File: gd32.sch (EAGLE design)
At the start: 23 parts, among them IC1 GD32F450IKH6, IC2 AMS1117-1.5, J1 LCD, U1 W9825G6KH-5

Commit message: Incremental changes
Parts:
- added BOOT_SEL: B3F-1005, SparkFun:TAC_SWITCHPTH
- added BOOT_WHICH: JS202011SCQN, samacsys:JS202011SCQN
- added C10, C9: 10uF/16v, rcl:C-EUC0603
- added C11: 0.1uF, rcl:C-EUC0201
- added D1: GRN-0402, Seeed-LED:SMD-LED-CLEAR-BLUE(0402)
- added JP2: (no value), pinhead:PINHD-1X2
- added R4: 470R, rcl:R-EU_R0402
- added R5: 10K, rcl:R-EU_R0402
- added U$1: GD32_DEBUG, sjg-stm32:GD32_DEBUG
- IC2: value AMS1117-1.5 -> AMS1117-3.3
- renumbered POWER1 to +5V_IN
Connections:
- new net BOOT0: BOOT_SEL.3, BOOT_SEL.4, IC1.BOOT0, R5.2
- new net N$2: D1.+, R4.2
- new net N$3: C10.1, IC2.TAB, IC2.VOUT, JP2.2, R4.1
- net +3V3: now also BOOT_SEL.1, BOOT_SEL.2, BOOT_WHICH.1, BOOT_WHICH.6, JP2.1, U$1.VDD_OUT@1; no longer IC2.TAB, IC2.VOUT
- net +5V: now also C9.1
- net GND: now also BOOT_WHICH.3, BOOT_WHICH.4, C10.2, C11.2, C9.2, R5.1, U$1.GND@3, U$1.GND@5, U$1.GND@9
- net PA13: now also U$1.SWDIO@2
- net PA14: now also U$1.SWD_CLK@4
- net PB10: now also U$1.USART_TX@6
- net PB11: now also U$1.USART_RX@8
- net PB2: now also BOOT_WHICH.2, BOOT_WHICH.5
- net PB4: now also C11.1, U$1.!RESET!@10
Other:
- moved on the sheet: C1, C2, C3, C4, C5, C6, C7, U1

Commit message: Ready for manufacture
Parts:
- removed C11: 0.1uF, rcl:C-EUC0201
- removed U$1: GD32_DEBUG, sjg-stm32:GD32_DEBUG
- added C12, C13: 15pF, rcl:C-EUC0201
- added C14, C15, C16, C17, C18, C19, C20, C21, C22, C23, C24, C25, C26, C27, C28, C34: 0.1uF, rcl:C-EUC0201
- added I2C1, SPI0, SPI1, SPI2: (no value), pinhead:PINHD-2X2
- added IO_EXT: (no value), pinhead:PINHD-2X20
- added PASS_RST: (no value), pinhead:PINHD-1X2
- added PROG: GD32_DEBUG, sjg-stm32:GD32_DEBUG
- added Q2: 8MHz, adafruit:XTAL-4-3225
- added R37, R8: 1K5, rcl:R-EU_R0603
- added R6, R7: 10K, rcl:R-EU_R0402
- added RESET: B3F-1005, SparkFun:TAC_SWITCHPTH
- R2, R3: device rcl:R-EU_R0805 -> rcl:R-EU_R0402; USE RMCF0805FT22R0 -> CR0402-JW-220GLF
- renumbered JP1 to BL_CTRL, JP2 to PASS_3V3
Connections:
- net PA11 renamed MCU_USB_N
- net PA12 renamed MCU_USB_P
- removed net PB4: C11.1, IC1.PB4, U$1.!RESET!@10
- removed net PD13: IC1.PD13
- removed net PE2: IC1.PE2
- removed net PE3: IC1.PE3
- removed net PG13: IC1.PG13
- removed net PG14: IC1.PG14, U1.!CAS
- removed net PG3: IC1.PG3
- removed net PG9: IC1.PG9
- removed net PH6: IC1.PH6
- removed net PH7: IC1.PH7
- removed net PI11: IC1.PI11
- new net !RST!: IC1.!RST!, PASS_RST.2, R7.1, RESET.3, RESET.4
- new net N$4: IC1.PDR_ON, R6.1
- new net N$5: PASS_RST.1, PROG.!RESET!@10
- net +3V3: now also C14.1, C15.1, C16.1, C17.1, C18.1, C19.1, C20.1, C21.1, C22.1, C23.1, C24.1, C25.1, C26.1, C27.1, C28.1, C34.1, I2C1.1, IC1.VBAT, IC1.VDD@C5, IC1.VDD@C7, IC1.VDD@C8, IC1.VDD@C9, IC1.VDD@F3, IC1.VDD@G13, IC1.VDD@G3, IC1.VDD@H13, IC1.VDD@J12, IC1.VDD@J13, IC1.VDD@K4, IC1.VDD@N10, IC1.VDD@N8, IC1.VDD@N9, IC1.VDDA, IC1.VREF+, IO_EXT.2, PROG.VDD_OUT@1, R37.2, R6.2, R7.2, R8.2; no longer U$1.VDD_OUT@1
- net +5V: now also IO_EXT.1
- net GND: now also C12.2, C13.2, C14.2, C15.2, C16.2, C17.2, C18.2, C19.2, C20.2, C21.2, C22.2, C23.2, C24.2, C25.2, C26.2, C27.2, C28.2, C34.2, D1.-, I2C1.3, IC1.VREF-, IC1.VSS@D5, IC1.VSS@D7, IC1.VSS@D8, IC1.VSS@D9, IC1.VSS@F10, IC1.VSS@F12, IC1.VSS@F2, IC1.VSS@F6, IC1.VSS@F7, IC1.VSS@F8, IC1.VSS@F9, IC1.VSS@G10, IC1.VSS@G12, IC1.VSS@G2, IC1.VSS@G6, IC1.VSS@G7, IC1.VSS@G8, IC1.VSS@G9, IC1.VSS@H10, IC1.VSS@H12, IC1.VSS@H6, IC1.VSS@H7, IC1.VSS@H8, IC1.VSS@H9, IC1.VSS@J10, IC1.VSS@J6, IC1.VSS@J7, IC1.VSS@J8, IC1.VSS@J9, IC1.VSS@K10, IC1.VSS@K6, IC1.VSS@K7, IC1.VSS@K8, IC1.VSS@K9, IC1.VSS@M8, IC1.VSS@M9, IC1.VSSA, IO_EXT.19, IO_EXT.20, IO_EXT.39, IO_EXT.40, PROG.GND@3, PROG.GND@5, PROG.GND@9, Q2.G1, Q2.G2, RESET.1, RESET.2, SPI0.3, SPI1.3, SPI2.3; no longer C11.2, U$1.GND@3, U$1.GND@5, U$1.GND@9
- net PA0: now also IO_EXT.37
- net PA1: now also IO_EXT.38
- net PA13: now also PROG.SWDIO@2; no longer U$1.SWDIO@2
- net PA14: now also PROG.SWD_CLK@4; no longer U$1.SWD_CLK@4
- net PA15: now also IO_EXT.31
- net PA2: now also IO_EXT.35
- net PA3: now also IO_EXT.36
- net PA5: now also SPI0.2
- net PA6: now also SPI0.4
- net PA7: now also SPI0.1
- net PA8: now also IO_EXT.33
- net PA9: now also IO_EXT.34
- net PB0: now also IO_EXT.32
- net PB1: now also IO_EXT.29
- net PB10: now also PROG.USART_TX@6; no longer U$1.USART_TX@6
- net PB11: now also PROG.USART_RX@8; no longer U$1.USART_RX@8
- net PB12: now also IO_EXT.26
- net PB13: now also SPI1.2
- net PB14: now also SPI1.4
- net PB15: now also SPI1.1
- net PB3: now also IO_EXT.30
- net PB7: now also IO_EXT.27
- net PB8: now also IO_EXT.28
- net PB9: now also IO_EXT.25
- net PC0: now also IO_EXT.23
- net PC1: now also IO_EXT.24
- net PC10: now also SPI2.2
- net PC11: now also SPI2.4
- net PC12: now also SPI2.1
- net PC13: now also IO_EXT.11
- net PC14: now also IO_EXT.12
- net PC15: now also IO_EXT.9
- net PC2: now also IO_EXT.21
- net PC3: now also IO_EXT.22
- net PC4: now also IO_EXT.17
- net PC5: now also IO_EXT.18
- net PC6: now also IO_EXT.15
- net PC7: now also IO_EXT.16
- net PC8: now also IO_EXT.13
- net PC9: now also IO_EXT.14
- net PD11: now also IO_EXT.3
- net PD12: now also IO_EXT.4
- net PD2: now also IO_EXT.10
- net PD3: now also IO_EXT.7
- net PD4: now also IO_EXT.8
- net PD6: now also IO_EXT.5
- net PD7: now also IO_EXT.6
- net PG15: now also U1.!CAS
- net PH0: now also C12.1, Q2.X1; no longer J1.!RST!@40
- net PH1: now also C13.1, Q2.X2; no longer J1.TP_IRQ@39
- net PH4: now also I2C1.2, R8.1
- net PH5: now also I2C1.4, R37.1
- net PI3: now also J1.!RST!@40
- net PI8: now also J1.TP_IRQ@39
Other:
- note added: "- Checked pinouts on: o LCD o SWDIO o I2C o SPI1, SPI2, SPI3 o SDRAM"
- note added: "CPU decoupling"
- note added: "SDRAM decoupling"
- note added: "Using CKE/EN on SDRAM #1"
- moved on the sheet: C1, C2, C3, C4, C5, C6, C7, IC1, J1, U1

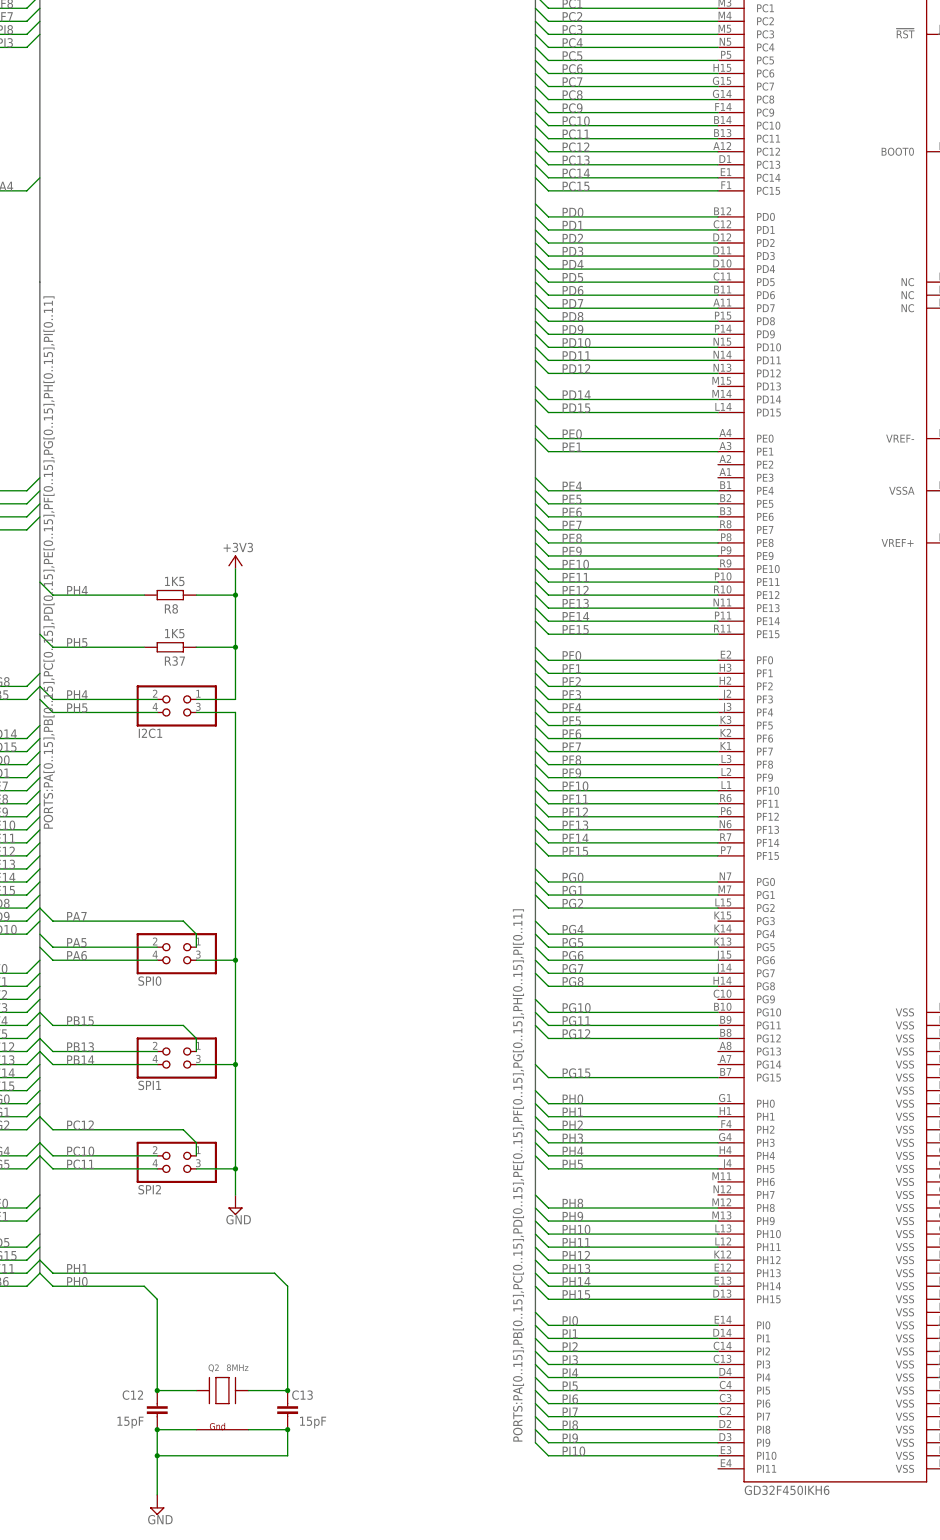
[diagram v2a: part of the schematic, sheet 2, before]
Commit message: Sent off for manufacture, with corrected 1K5 pullups on I2C
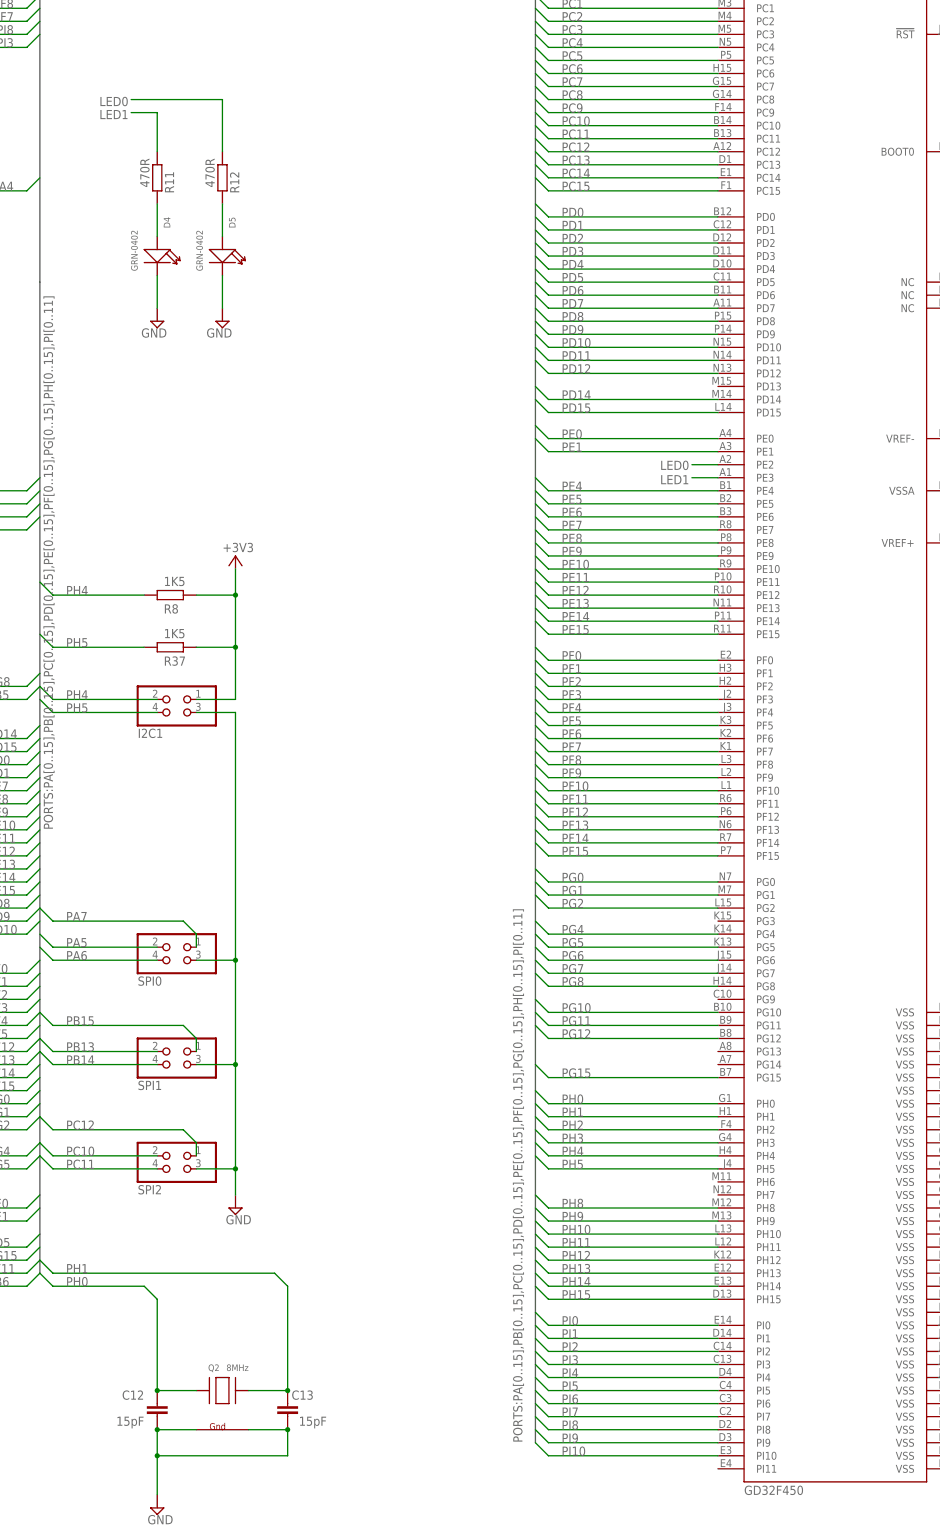
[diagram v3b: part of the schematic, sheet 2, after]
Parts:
- added D4, D5: GRN-0402, Seeed-LED:SMD-LED-CLEAR-BLUE(0402)
- added R11, R12: 470R, rcl:R-EU_R0402
- IC1: value GD32F450IKH6 -> GD32F450
- PROG: USE (none) -> FTSH-105-01-LM-DV-K-P-TR
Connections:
- new net LED0: IC1.PE2, R12.1
- new net LED1: IC1.PE3, R11.1
- new net N$8: D4.+, R11.2
- new net N$9: D5.+, R12.2
- net GND: now also D4.-, D5.-

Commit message: Persist the correct new pullup parts in the USE tags of the schematic components
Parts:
- R37, R8: USE ERJ-1GNJ472C -> WR06X152 JTL
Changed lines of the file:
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@@
 </pinmapping>
 </spice>
-<attribute name="USE" value="ERJ-1GNJ472C"/>
+<attribute name="USE" value="WR06X152 JTL"/>
 </part>
 <part name="R8" library="rcl" library_urn="urn:adsk.eagle:library:334" deviceset="R-EU_" device="R0603" package3d_urn="urn:adsk.eagle:package:23555/3" value="1K5">
@@
 </pinmapping>
 </spice>
-<attribute name="USE" value="ERJ-1GNJ472C"/>
+<attribute name="USE" value="WR06X152 JTL"/>
 </part>
 <part name="PASS_RST" library="pinhead" library_urn="urn:adsk.eagle:library:325" deviceset="PINHD-1X2" device="" package3d_urn="urn:adsk.eagle:package:22435/2"/>

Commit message: Alter the pad sizes in the GD32 library
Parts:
- IC1: device samacsys:GD32F450IKH6 -> gd32:GD32F450II
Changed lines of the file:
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@@
 <attribute name="USE" value="CR0402-JW-220GLF"/>
 </part>
-<part name="IC1" library="samacsys" deviceset="GD32F450IKH6" device="" value="GD32F450"/>
+<part name="IC1" library="gd32" deviceset="GD32F450II" device="" value="GD32F450"/>
 <part name="FRAME2" library="frames" library_urn="urn:adsk.eagle:library:229" deviceset="FRAME_C_L" device=""/>
 <part name="FRAME1" library="frames" library_urn="urn:adsk.eagle:library:229" deviceset="A3L-LOC" device=""/>
